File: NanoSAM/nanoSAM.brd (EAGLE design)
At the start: 95.9 x 90.2 mm, 91 parts, among them IC3 AD5241, J1 POWER_JACK, U1 LTC3260EMSEPBF

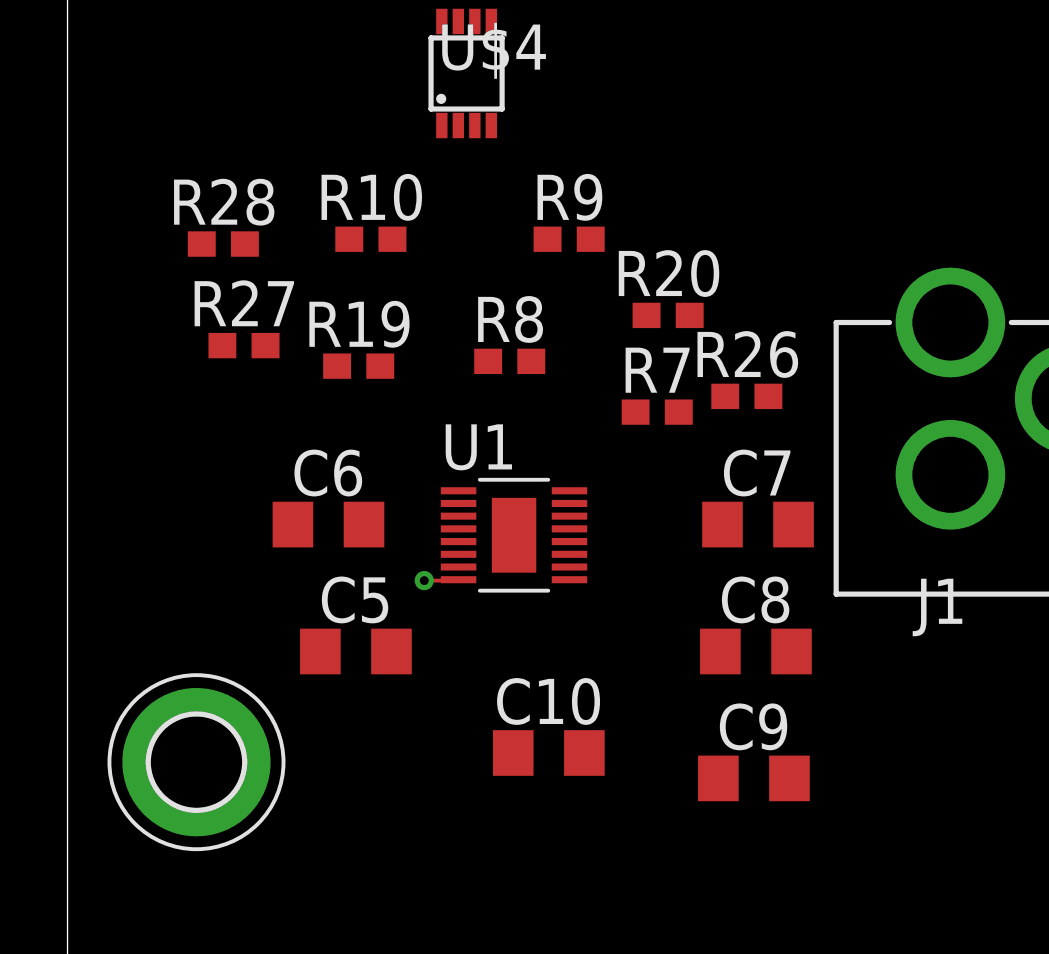
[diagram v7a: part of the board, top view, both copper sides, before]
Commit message: Edited Bipolar power supply
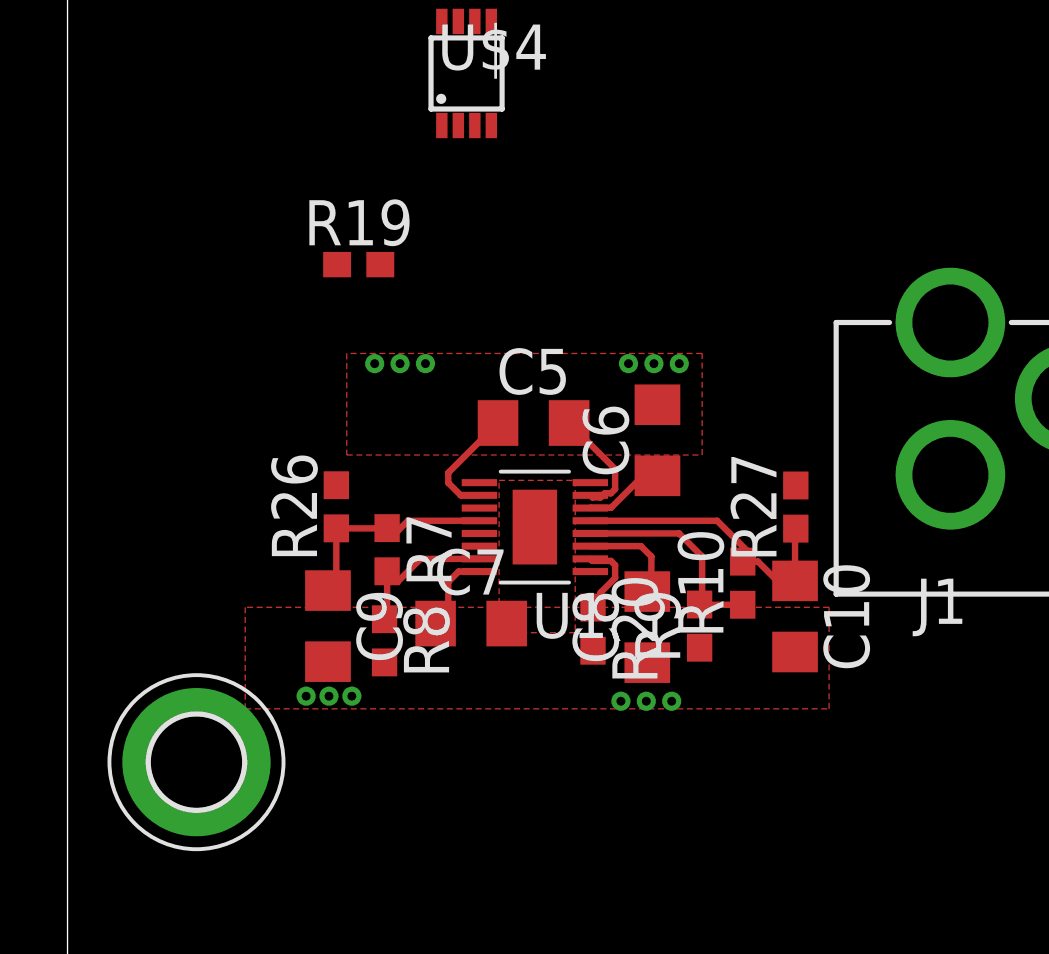
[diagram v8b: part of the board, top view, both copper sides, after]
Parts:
- removed R28: 0, SparkFun-Resistors:0603
- moved R27 22.7 mm to (28.7, 18.9), turned to 90 degrees
- moved R10 20.0 mm to (26.6, 15.9), turned to 90 degrees
- moved C9 17.8 mm to (10.3, 14.3), turned to 270 degrees
- moved R26 16.7 mm to (10.6, 19.0), turned to 90 degrees
- moved R9 16.1 mm to (24.9, 14.3), turned to 90 degrees
- moved C6 13.4 mm to (23.2, 21.6), turned to 90 degrees
- moved R20 12.7 mm to (20.7, 14.1), turned to 270 degrees
- moved R8 12.1 mm to (12.5, 13.7), turned to 270 degrees
- moved C7 12.0 mm to (15.9, 14.4)
- moved R7 11.9 mm to (12.6, 17.3), turned to 270 degrees
- moved C5 11.4 mm to (18.4, 22.3)
- moved C10 11.1 mm to (28.7, 14.6), turned to 270 degrees
- moved C8 4.39 mm to (22.8, 14.2), turned to 90 degrees
- moved R19 4.00 mm to (11.5, 28.5)
- moved U1 0.88 mm to (18.4, 18.2), turned to 180 degrees
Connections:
- removed net N$26: C7.2, C8.1, R28.1, R8.2, R9.1, U1.17
- net AGND: now also C7.2, C8.1, R8.2, R9.1, U1.17; no longer R28.2
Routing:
- net N$24: track 0.00 -> 12.0 mm
- net N$22: track 0.00 -> 8.45 mm
- net N$12: track 0.00 -> 8.39 mm
- net N$7: track 0.00 -> 6.12 mm
- net N$18: track 0.00 -> 4.60 mm
- net N$19: track 0.00 -> 4.50 mm
- net N$14: track 0.00 -> 4.02 mm
- net N$23: track 0.00 -> 3.28 mm
- net N$6: track 0.00 -> 3.24 mm
- net N$10: track 0.00 -> 3.17 mm
- net AGND: track 8.69 -> 7.32 mm, vias 5 -> 16
- added copper zone on layer 1, net AGND
